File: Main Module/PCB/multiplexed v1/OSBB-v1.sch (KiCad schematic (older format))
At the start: 32 parts, among them P1 AUX 1, P10 +3.3V Pins, P11 BTN-1-4, P12 BTN-5-8, P13 BTN-9-12, P14 EXTRA Pins, P15 BTN-17-20, P16 BTN-13-16, P17 BTN-25-28, P18 BTN-21-24, P19 BTN-29-32, P2 AUX 2, P3 AUX 3, P4 Pit limiter, P5 Rotary Encoders, P6 GND Pins, P7 Teensy 3.1 left, P8 +5V, P9 Teensy 3.1 right, Q1 Q_NPN_CBE, Q2 Q_NPN_CBE, Q3 Q_NPN_CBE, U1 74HC4051, U2 74HC4051, U3 74HC4051, U4 74HC4051

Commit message: * created Teensy 3.2 library part (very basic)
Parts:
- removed P7: Teensy 3.1 left, Socket_Strips:Socket_Strip_Straight_1x14, symbol CONN_01X14
- removed P8: +5V, Pin_Headers:Pin_Header_Straight_1x01, symbol CONN_01X01
- removed P9: Teensy 3.1 right, Socket_Strips:Socket_Strip_Straight_1x14, symbol CONN_01X14
- added U5: Teensy3.2, Housings_DIP:DIP-28_W15.24mm_LongPads, symbol Teensy3.2
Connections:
- net labels removed: 3.3V
- wire segments 207 -> 196
- no-connect marks 4 -> 9
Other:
- moved on the sheet: P10, P14
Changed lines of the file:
@@
 LIBS:valves
 LIBS:74hc4051
+LIBS:Teensy3.2
 LIBS:OSBB-v1-cache
 EELAYER 25 0
@@
 $EndDescr
 $Comp
-L CONN_01X14 P7
-U 1 1 57F0D936
-P 4650 5100
-F 0 "P7" H 4650 5850 50  0000 C CNN
-F 1 "Teensy 3.1 left" V 4750 5100 50  0000 C CNN
-F 2 "Socket_Strips:Socket_Strip_Straight_1x14" H 4650 5100 50  0001 C CNN
-F 3 "" H 4650 5100 50  0000 C CNN
-	1    4650 5100
-	1    0    0    -1
-$EndComp
-$Comp
 L CONN_01X03 P6
 U 1 1 57F0DE17
@@
 L CONN_01X03 P10
 U 1 1 57F0DFEC
-P 5750 4200
-F 0 "P10" H 5750 4400 50  0000 C CNN
-F 1 "+3.3V Pins" V 5850 4200 50  0000 C CNN
-F 2 "Pin_Headers:Pin_Header_Angled_1x03" H 5750 4200 50  0001 C CNN
-F 3 "" H 5750 4200 50  0000 C CNN
-	1    5750 4200
+P 7000 4450
+F 0 "P10" H 7000 4650 50  0000 C CNN
+F 1 "+3.3V Pins" V 7100 4450 50  0000 C CNN
+F 2 "Pin_Headers:Pin_Header_Angled_1x03" H 7000 4450 50  0001 C CNN
+F 3 "" H 7000 4450 50  0000 C CNN
+	1    7000 4450
 	0    -1   -1   0
 $EndComp
-Text Label 5650 4650 0    60   ~ 0
-3.3V
 Text Label 4200 4400 0    60   ~ 0
 GND
@@
 	-1   0    0    1
 $EndComp
-$Comp
-L CONN_01X01 P8
-U 1 1 57F1C39A
-P 4950 4450
-F 0 "P8" H 4950 4550 50  0000 C CNN
-F 1 "+5V" V 5050 4450 50  0000 C CNN
-F 2 "Pin_Headers:Pin_Header_Straight_1x01" H 4950 4450 50  0001 C CNN
-F 3 "" H 4950 4450 50  0000 C CNN
-	1    4950 4450
-	0    1    1    0
-$EndComp
-$Comp
-L +5V #PWR07
-U 1 1 57F1C66D
-P 4950 4150
-F 0 "#PWR07" H 4950 4000 50  0001 C CNN
-F 1 "+5V" H 4950 4290 50  0000 C CNN
-F 2 "" H 4950 4150 50  0000 C CNN
-F 3 "" H 4950 4150 50  0000 C CNN
-	1    4950 4150
-	1    0    0    -1
-$EndComp
-Text Label 5300 5150 0    60   ~ 0
+Text Label 5950 5150 0    60   ~ 0
 reserved_for_4051
-NoConn ~ 5300 4450
-NoConn ~ 5300 4550
-NoConn ~ 5300 5750
-$Comp
-L CONN_01X14 P9
-U 1 1 57F0DAC4
-P 5100 5100
-F 0 "P9" H 5100 5850 50  0000 C CNN
-F 1 "Teensy 3.1 right" V 5200 5100 50  0000 C CNN
-F 2 "Socket_Strips:Socket_Strip_Straight_1x14" H 5100 5100 50  0001 C CNN
-F 3 "" H 5100 5100 50  0000 C CNN
-	1    5100 5100
-	-1   0    0    -1
-$EndComp
 $Comp
 L CONN_01X05 P14
 U 1 1 580F60D7
-P 5950 5700
-F 0 "P14" H 5950 6000 50  0000 C CNN
-F 1 "EXTRA Pins" V 6050 5700 50  0000 C CNN
-F 2 "Pin_Headers:Pin_Header_Angled_1x05" H 5950 5700 50  0001 C CNN
-F 3 "" H 5950 5700 50  0000 C CNN
-	1    5950 5700
-	1    0    0    -1
-$EndComp
-NoConn ~ 5300 5150
+P 6900 5450
+F 0 "P14" H 6900 5750 50  0000 C CNN
+F 1 "EXTRA Pins" V 7000 5450 50  0000 C CNN
+F 2 "Pin_Headers:Pin_Header_Angled_1x05" H 6900 5450 50  0001 C CNN
+F 3 "" H 6900 5450 50  0000 C CNN
+	1    6900 5450
+	1    0    0    -1
+$EndComp
 $Comp
 L 74HC4051 U2
@@
 $EndComp
 $Comp
-L GND #PWR08
+L GND #PWR07
 U 1 1 580F9CCA
 P 1400 2150
-F 0 "#PWR08" H 1400 1900 50  0001 C CNN
+F 0 "#PWR07" H 1400 1900 50  0001 C CNN
 F 1 "GND" H 1400 2000 50  0000 C CNN
 F 2 "" H 1400 2150 50  0000 C CNN
@@
 $EndComp
 $Comp
-L GND #PWR09
+L GND #PWR08
 U 1 1 580F9D12
 P 4550 3550
-F 0 "#PWR09" H 4550 3300 50  0001 C CNN
+F 0 "#PWR08" H 4550 3300 50  0001 C CNN
 F 1 "GND" H 4550 3400 50  0000 C CNN
 F 2 "" H 4550 3550 50  0000 C CNN
@@
 $EndComp
 $Comp
-L GND #PWR010
+L GND #PWR09
 U 1 1 580F9D5A
 P 6700 2250
-F 0 "#PWR010" H 6700 2000 50  0001 C CNN
+F 0 "#PWR09" H 6700 2000 50  0001 C CNN
 F 1 "GND" H 6700 2100 50  0000 C CNN
 F 2 "" H 6700 2250 50  0000 C CNN
@@
 $EndComp
 $Comp
-L GND #PWR011
+L GND #PWR010
 U 1 1 580FA3EE
 P 8300 3350
-F 0 "#PWR011" H 8300 3100 50  0001 C CNN
+F 0 "#PWR010" H 8300 3100 50  0001 C CNN
 F 1 "GND" H 8300 3200 50  0000 C CNN
 F 2 "" H 8300 3350 50  0000 C CNN
@@
 $EndComp
 $Comp
-L +3.3V #PWR012
+L +3.3V #PWR011
 U 1 1 580FAACB
 P 2200 650
-F 0 "#PWR012" H 2200 500 50  0001 C CNN
+F 0 "#PWR011" H 2200 500 50  0001 C CNN
 F 1 "+3.3V" H 2200 790 50  0000 C CNN
 F 2 "" H 2200 650 50  0000 C CNN
@@
 $EndComp
 $Comp
-L +3.3V #PWR013
+L +3.3V #PWR012
 U 1 1 580FAB13
 P 7600 650
-F 0 "#PWR013" H 7600 500 50  0001 C CNN
+F 0 "#PWR012" H 7600 500 50  0001 C CNN
 F 1 "+3.3V" H 7600 790 50  0000 C CNN
 F 2 "" H 7600 650 50  0000 C CNN
@@
 $EndComp
 $Comp
-L +3.3V #PWR014
+L +3.3V #PWR013
 U 1 1 580FAB5B
 P 9200 1750
-F 0 "#PWR014" H 9200 1600 50  0001 C CNN
+F 0 "#PWR013" H 9200 1600 50  0001 C CNN
 F 1 "+3.3V" H 9200 1890 50  0000 C CNN
 F 2 "" H 9200 1750 50  0000 C CNN
@@
 $EndComp
 $Comp
-L +3.3V #PWR015
+L +3.3V #PWR014
 U 1 1 580FABA3
 P 5450 1750
-F 0 "#PWR015" H 5450 1600 50  0001 C CNN
+F 0 "#PWR014" H 5450 1600 50  0001 C CNN
 F 1 "+3.3V" H 5450 1890 50  0000 C CNN
 F 2 "" H 5450 1750 50  0000 C CNN
@@
 $EndComp
 Wire Wire Line
-	5300 4750 6200 4750
-Wire Wire Line
 	6200 4750 6200 3800
 Wire Wire Line
-	5300 4850 6350 4850
-Wire Wire Line
-	6550 4950 5300 4950
-Wire Wire Line
 	6550 1300 6550 4950
 Wire Wire Line
-	5300 5050 7850 5050
-Wire Wire Line
 	2200 2050 9350 2050
 Wire Wire Line
 	3350 2050 3350 4550
 Wire Wire Line
-	3350 4550 4450 4550
+	3350 4550 4550 4550
 Connection ~ 3350 2050
 Wire Wire Line
@@
 	3450 2000 3450 4650
 Wire Wire Line
-	3450 4650 4450 4650
+	3450 4650 4550 4650
 Connection ~ 3450 2000
 Wire Wire Line
@@
 	2300 1950 9450 1950
 Wire Wire Line
-	3550 4750 4450 4750
+	3550 4750 4550 4750
 Connection ~ 3550 1950
 Wire Wire Line
@@
 	2950 6400 2950 6550
 Wire Wire Line
-	3900 5750 4450 5750
-Wire Wire Line
-	3900 5650 4450 5650
-Wire Wire Line
-	3900 5550 4450 5550
-Wire Wire Line
-	3900 5450 4450 5450
-Wire Wire Line
-	3900 5350 4450 5350
-Wire Wire Line
-	3900 5250 4450 5250
-Wire Wire Line
-	4950 4250 4950 4150
-Wire Wire Line
-	4450 4850 1200 4850
+	3900 5750 4550 5750
+Wire Wire Line
+	3900 5650 4550 5650
+Wire Wire Line
+	3900 5550 4550 5550
+Wire Wire Line
+	3900 5450 4550 5450
+Wire Wire Line
+	3900 5350 4550 5350
+Wire Wire Line
+	3900 5250 4550 5250
+Wire Wire Line
+	1200 4850 4550 4850
 Wire Wire Line
 	1200 4850 1200 5400
 Wire Wire Line
-	4450 4950 1950 4950
+	1950 4950 4550 4950
 Wire Wire Line
 	1950 4950 1950 5400
 Wire Wire Line
-	4450 5050 2650 5050
+	2650 5050 4550 5050
 Wire Wire Line
 	2650 5050 2650 5400
 Wire Wire Line
-	4450 5150 3100 5150
+	3100 5150 4550 5150
 Wire Wire Line
 	3100 5150 3100 5550
@@
 Connection ~ 4100 4400
 Connection ~ 4000 4400
-Wire Wire Line
-	5300 5650 5350 5650
-Wire Wire Line
-	5350 5650 5350 5900
-Wire Wire Line
-	5350 5900 5750 5900
-Wire Wire Line
-	5300 5550 5400 5550
-Wire Wire Line
-	5400 5550 5400 5800
-Wire Wire Line
-	5400 5800 5750 5800
-Wire Wire Line
-	5300 5450 5450 5450
-Wire Wire Line
-	5450 5450 5450 5700
-Wire Wire Line
-	5450 5700 5750 5700
-Wire Wire Line
-	5300 5350 5500 5350
-Wire Wire Line
-	5500 5350 5500 5600
-Wire Wire Line
-	5500 5600 5750 5600
-Wire Wire Line
-	5300 5250 5550 5250
-Wire Wire Line
-	5550 5250 5550 5500
-Wire Wire Line
-	5550 5500 5750 5500
-Wire Wire Line
-	5300 4650 5650 4650
-Wire Wire Line
-	5650 4650 5650 4400
-Wire Wire Line
-	5650 4400 5850 4400
-Connection ~ 5750 4400
-Connection ~ 5650 4400
 Wire Wire Line
 	7850 5050 7850 2550
@@
 $EndComp
 $Comp
-L GND #PWR016
+L GND #PWR015
 U 1 1 5810375B
 P 2950 5400
-F 0 "#PWR016" H 2950 5150 50  0001 C CNN
+F 0 "#PWR015" H 2950 5150 50  0001 C CNN
 F 1 "GND" H 2950 5250 50  0000 C CNN
 F 2 "" H 2950 5400 50  0000 C CNN
@@
 $EndComp
 $Comp
-L +5V #PWR017
+L +5V #PWR016
 U 1 1 581037AF
 P 3300 5500
-F 0 "#PWR017" H 3300 5350 50  0001 C CNN
+F 0 "#PWR016" H 3300 5350 50  0001 C CNN
 F 1 "+5V" H 3300 5640 50  0000 C CNN
 F 2 "" H 3300 5500 50  0000 C CNN
@@
 Wire Wire Line
 	3300 5550 3300 5500
+$Comp
+L Teensy3.2 U5
+U 1 1 5810D118
+P 5250 5050
+F 0 "U5" H 4800 5800 60  0000 C CNN
+F 1 "Teensy3.2" H 4950 5900 60  0000 C CNN
+F 2 "Housings_DIP:DIP-28_W15.24mm_LongPads" H 5250 5650 60  0001 C CNN
+F 3 "" H 5250 5650 60  0001 C CNN
+	1    5250 5050
+	1    0    0    -1
+$EndComp
+Wire Wire Line
+	4450 4450 4550 4450
+Wire Wire Line
+	5950 4750 6200 4750
+Wire Wire Line
+	5950 4850 6350 4850
+Wire Wire Line
+	6550 4950 5950 4950
+Wire Wire Line
+	5950 5050 7850 5050
+NoConn ~ 5950 5150
+NoConn ~ 5950 4450
+NoConn ~ 5950 4550
+NoConn ~ 5950 5750
+Wire Wire Line
+	5950 5250 6700 5250
+Wire Wire Line
+	6700 5350 5950 5350
+Wire Wire Line
+	5950 5450 6700 5450
+Wire Wire Line
+	6700 5550 5950 5550
+Wire Wire Line
+	5950 5650 6700 5650
+Wire Wire Line
+	5950 4650 7100 4650
+Connection ~ 6900 4650
+Connection ~ 7000 4650
+$Comp
+L +5V #PWR017
+U 1 1 581107FE
+P 5450 4000
+F 0 "#PWR017" H 5450 3850 50  0001 C CNN
+F 1 "+5V" H 5450 4140 50  0000 C CNN
+F 2 "" H 5450 4000 50  0000 C CNN
+F 3 "" H 5450 4000 50  0000 C CNN
+	1    5450 4000
+	1    0    0    -1
+$EndComp
+Wire Wire Line
+	5450 4050 5450 4000
+NoConn ~ 4950 6400
+NoConn ~ 5100 6400
+NoConn ~ 5250 6400
+NoConn ~ 5400 6400
+NoConn ~ 5550 6400
 $EndSCHEMATC

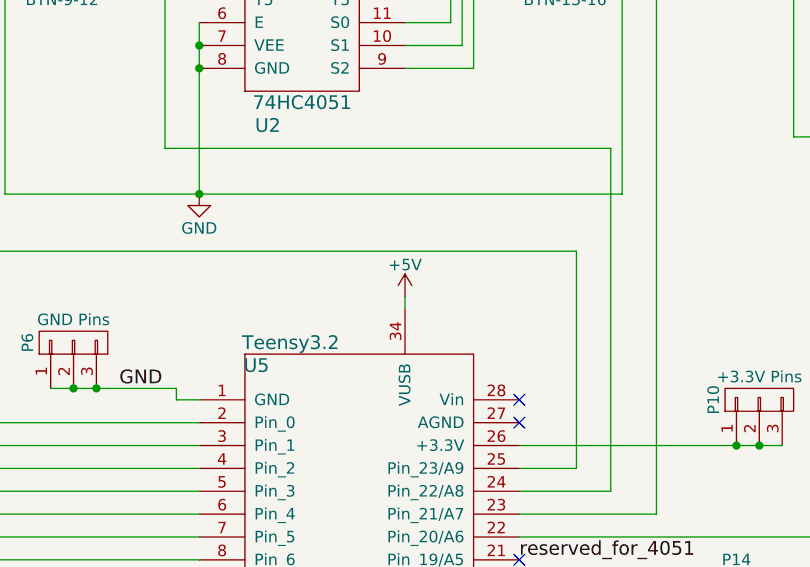
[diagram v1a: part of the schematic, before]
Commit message: * Added pin numbers to Teensy library part to match DIL-28 housing
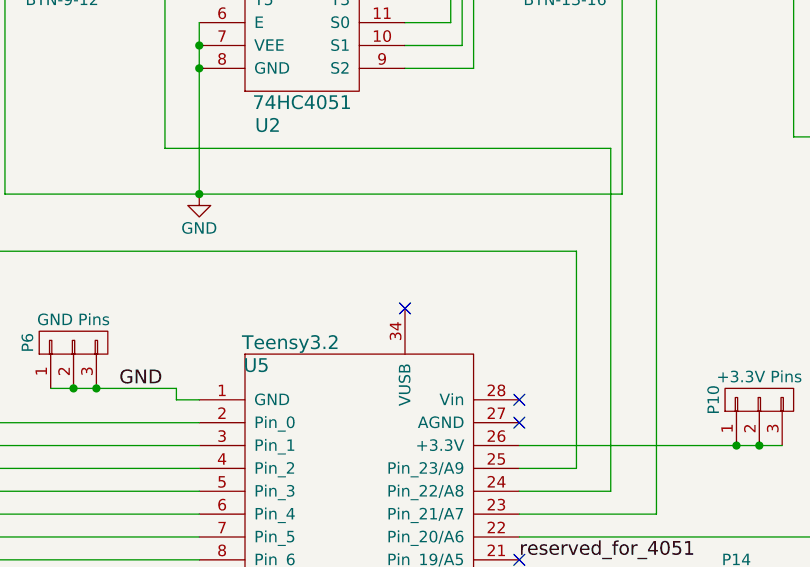
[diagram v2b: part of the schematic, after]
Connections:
- net +5V: no longer U5.34 (VUSB)
- no-connect marks 9 -> 10
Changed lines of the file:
@@
 EESchema Schematic File Version 2
+LIBS:OSBB-v1-rescue
 LIBS:power
 LIBS:device
@@
 Wire Wire Line
 	3300 5550 3300 5500
+Wire Wire Line
+	4450 4450 4550 4450
+Wire Wire Line
+	5950 4750 6200 4750
+Wire Wire Line
+	5950 4850 6350 4850
+Wire Wire Line
+	6550 4950 5950 4950
+Wire Wire Line
+	5950 5050 7850 5050
+NoConn ~ 5950 5150
+NoConn ~ 5950 4450
+NoConn ~ 5950 4550
+NoConn ~ 5950 5750
+Wire Wire Line
+	5950 5250 6700 5250
+Wire Wire Line
+	6700 5350 5950 5350
+Wire Wire Line
+	5950 5450 6700 5450
+Wire Wire Line
+	6700 5550 5950 5550
+Wire Wire Line
+	5950 5650 6700 5650
+Wire Wire Line
+	5950 4650 7100 4650
+Connection ~ 6900 4650
+Connection ~ 7000 4650
+NoConn ~ 4950 6400
+NoConn ~ 5100 6400
+NoConn ~ 5250 6400
+NoConn ~ 5400 6400
+NoConn ~ 5550 6400
 $Comp
 L Teensy3.2 U5
@@
 	1    0    0    -1
 $EndComp
-Wire Wire Line
-	4450 4450 4550 4450
-Wire Wire Line
-	5950 4750 6200 4750
-Wire Wire Line
-	5950 4850 6350 4850
-Wire Wire Line
-	6550 4950 5950 4950
-Wire Wire Line
-	5950 5050 7850 5050
-NoConn ~ 5950 5150
-NoConn ~ 5950 4450
-NoConn ~ 5950 4550
-NoConn ~ 5950 5750
-Wire Wire Line
-	5950 5250 6700 5250
-Wire Wire Line
-	6700 5350 5950 5350
-Wire Wire Line
-	5950 5450 6700 5450
-Wire Wire Line
-	6700 5550 5950 5550
-Wire Wire Line
-	5950 5650 6700 5650
-Wire Wire Line
-	5950 4650 7100 4650
-Connection ~ 6900 4650
-Connection ~ 7000 4650
-$Comp
-L +5V #PWR017
-U 1 1 581107FE
-P 5450 4000
-F 0 "#PWR017" H 5450 3850 50  0001 C CNN
-F 1 "+5V" H 5450 4140 50  0000 C CNN
-F 2 "" H 5450 4000 50  0000 C CNN
-F 3 "" H 5450 4000 50  0000 C CNN
-	1    5450 4000
-	1    0    0    -1
-$EndComp
-Wire Wire Line
-	5450 4050 5450 4000
-NoConn ~ 4950 6400
-NoConn ~ 5100 6400
-NoConn ~ 5250 6400
-NoConn ~ 5400 6400
-NoConn ~ 5550 6400
+NoConn ~ 5450 4050
 $EndSCHEMATC

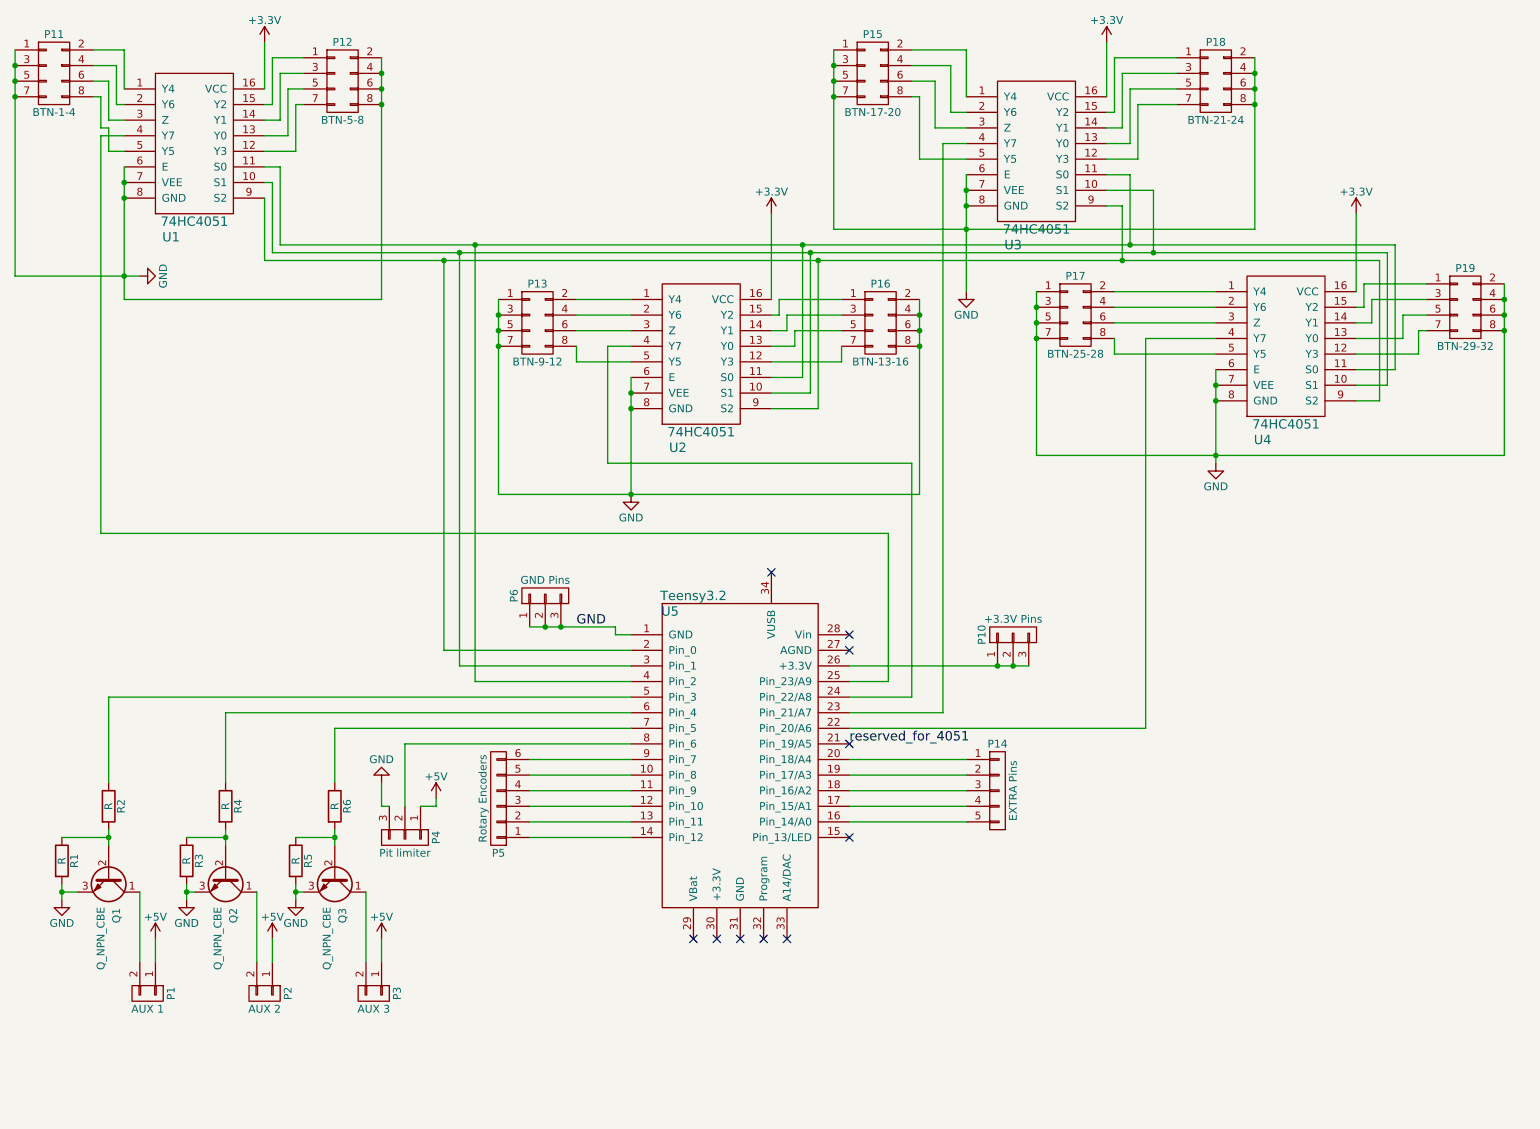
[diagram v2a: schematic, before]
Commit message: * changed pinout of headers for buttons. now consisten GND on 1,3,5,7
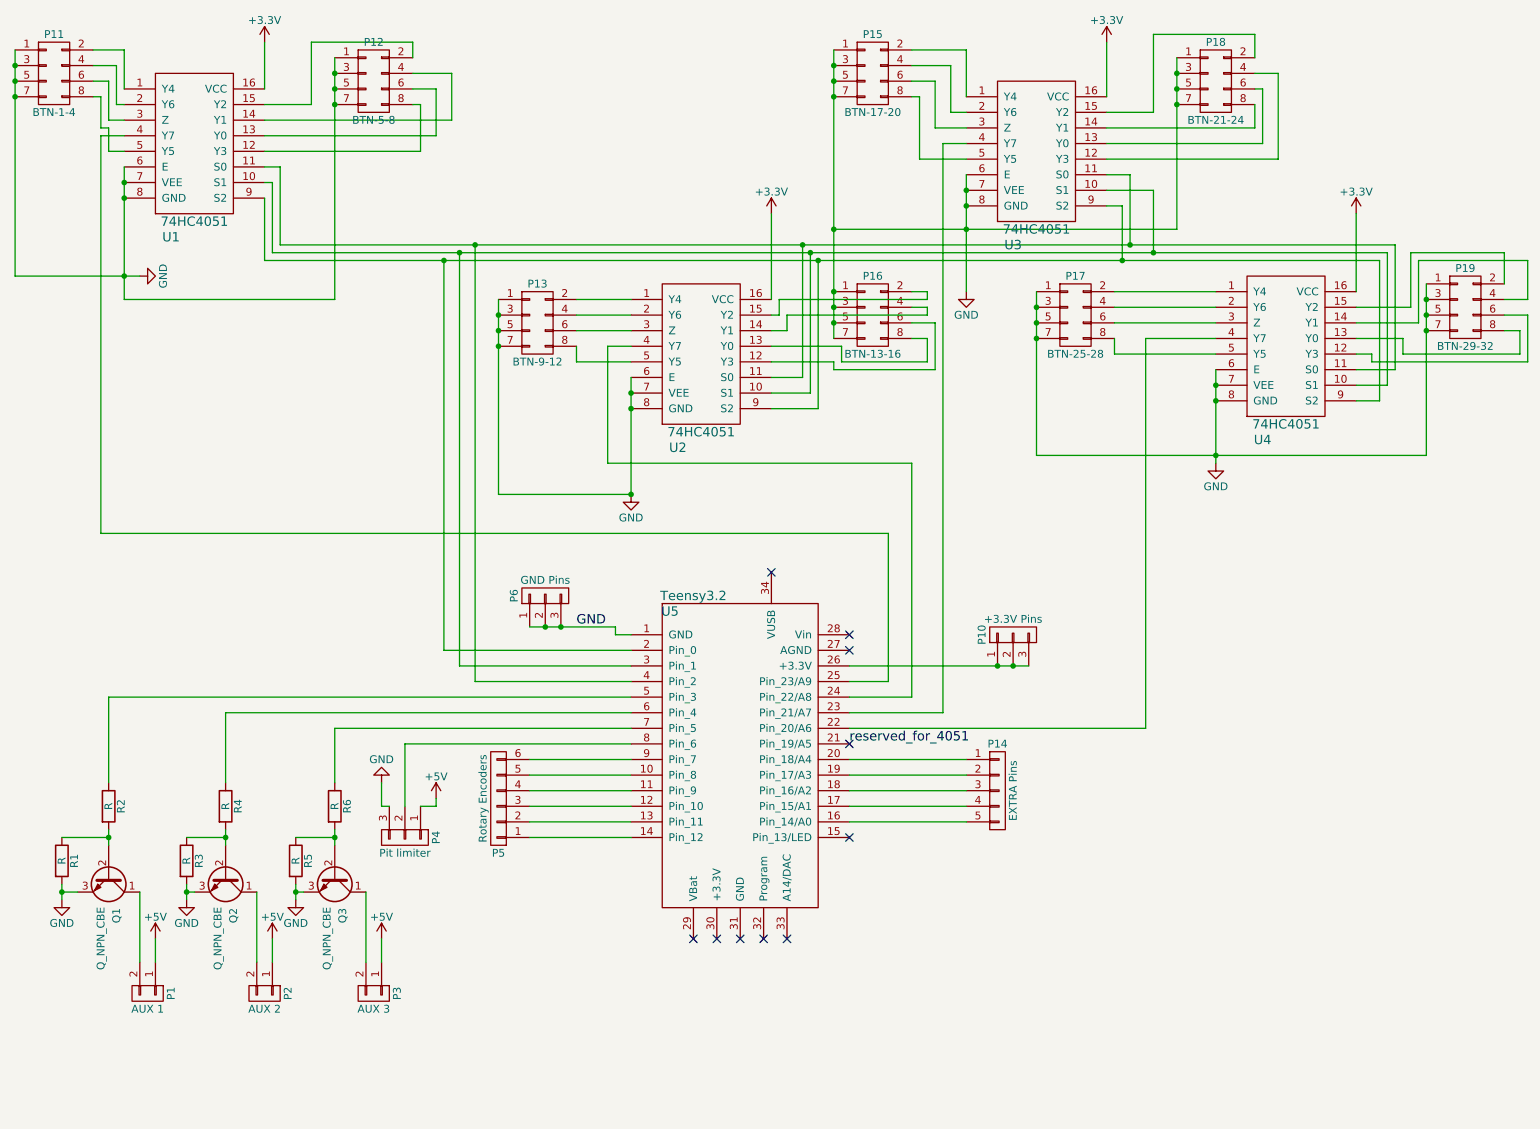
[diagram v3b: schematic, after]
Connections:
- net GND: now also P12.1 (P1), P12.3 (P3), P12.5 (P5), P12.7 (P7), P16.1 (P1), P16.3 (P3), P16.5 (P5), P16.7 (P7), P18.1 (P1), P18.3 (P3), P18.5 (P5), P18.7 (P7), P19.1 (P1), P19.3 (P3), P19.5 (P5), P19.7 (P7); no longer P12.2 (P2), P12.4 (P4), P12.6 (P6), P12.8 (P8), P16.2 (P2), P16.4 (P4), P16.6 (P6), P16.8 (P8), P18.2 (P2), P18.4 (P4), P18.6 (P6), P18.8 (P8), P19.2 (P2), P19.4 (P4), P19.6 (P6), P19.8 (P8)
- net at U2.12 (Y3): now also P16.6 (P6); no longer P16.7 (P7)
- net at U2.13 (Y0): now also P16.8 (P8); no longer P16.5 (P5)
- net at U2.14 (Y1): now also P16.4 (P4); no longer P16.3 (P3)
- net at U2.15 (Y2): now also P16.2 (P2); no longer P16.1 (P1)
- net at U3.12 (Y3): now also P18.4 (P4); no longer P18.7 (P7)
- net at U3.13 (Y0): now also P18.6 (P6); no longer P18.5 (P5)
- net at U3.14 (Y1): now also P18.8 (P8); no longer P18.3 (P3)
- net at U3.15 (Y2): now also P18.2 (P2); no longer P18.1 (P1)
- net at U1.12 (Y3): now also P12.8 (P8); no longer P12.7 (P7)
- net at U1.13 (Y0): now also P12.6 (P6); no longer P12.5 (P5)
- net at U1.14 (Y1): now also P12.4 (P4); no longer P12.3 (P3)
- net at U1.15 (Y2): now also P12.2 (P2); no longer P12.1 (P1)
- net at U4.12 (Y3): now also P19.6 (P6); no longer P19.7 (P7)
- net at U4.13 (Y0): now also P19.8 (P8); no longer P19.5 (P5)
- net at U4.14 (Y1): now also P19.4 (P4); no longer P19.3 (P3)
- net at U4.15 (Y2): now also P19.2 (P2); no longer P19.1 (P1)
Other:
- moved on the sheet: P12, P16
